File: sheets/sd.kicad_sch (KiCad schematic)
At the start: 1 part

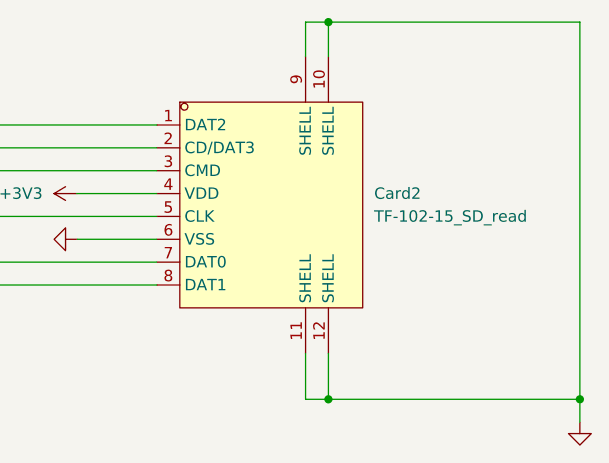
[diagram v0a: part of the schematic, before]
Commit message: added current rush limiting resistors to bmp581
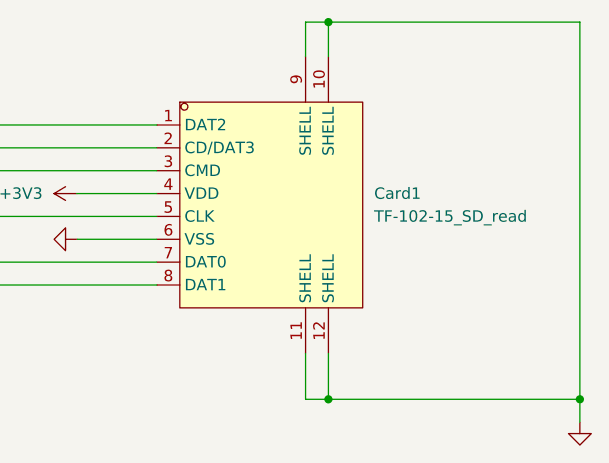
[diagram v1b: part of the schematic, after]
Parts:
- renumbered Card2 to Card1
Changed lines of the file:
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@@
 		)
 		(instances
-			(project ""
+			(project "aerolotl"
 				(path "/3f5bc5ea-feaa-4ed9-b0e0-c918b1fb5754/5163456c-8297-491e-bf51-bada45954a82"
 					(reference "#PWR045")
@@
 		)
 		(instances
-			(project "nc_fc"
+			(project "aerolotl"
 				(path "/3f5bc5ea-feaa-4ed9-b0e0-c918b1fb5754/5163456c-8297-491e-bf51-bada45954a82"
 					(reference "#PWR046")
@@
 		(dnp no)
 		(fields_autoplaced yes)
-		(property "Reference" "Card2"
+		(property "Reference" "Card1"
 			(at 177.8 100.3299 0)
 			(effects
@@
 			(project "aerolotl"
 				(path "/3f5bc5ea-feaa-4ed9-b0e0-c918b1fb5754/5163456c-8297-491e-bf51-bada45954a82"
-					(reference "Card2")
+					(reference "Card1")
 					(unit 1)
 				)
@@
 		)
 		(instances
-			(project ""
+			(project "aerolotl"
 				(path "/3f5bc5ea-feaa-4ed9-b0e0-c918b1fb5754/5163456c-8297-491e-bf51-bada45954a82"
 					(reference "#PWR044")

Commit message: added spi
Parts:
- added R17, R26, R27, R28, R29: 10k, symbol Device:R
- added R30, R31, R32, R33, R34, R35: 10, symbol Device:R
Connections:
- net +3V3: now also R17.1, R26.1, R27.1, R28.1, R29.1
- net SD.CK: now also R33.1; no longer Card1.5 (CLK)
- net SD.CMD: now also R32.1; no longer Card1.3 (CMD)
- net SD.D0: now also R34.1; no longer Card1.7 (DAT0)
- net SD.D1: now also R35.1; no longer Card1.8 (DAT1)
- net SD.D2: now also R30.1; no longer Card1.1 (DAT2)
- net SD.D3: now also R31.1; no longer Card1.2 (CD/DAT3)
- new net: Card1.7 (DAT0), R28.2, R34.2
- new net: Card1.2 (CD/DAT3), R26.2, R31.2
- new net: Card1.8 (DAT1), R29.2, R35.2
- new net: Card1.3 (CMD), R27.2, R32.2
- new net: Card1.1 (DAT2), R17.2, R30.2
- new net: Card1.5 (CLK), R33.2
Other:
- note added: "Note: make trace length short (< 2 inch from MCU to sd card reader)"
- moved on the sheet: Card1

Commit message: Rev1 schematic done
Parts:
- renumbered R35 to R28, R30 to R29, R31 to R30, R32 to R31, R33 to R32, R34 to R33, R29 to R34, R28 to R35, R27 to R36, R26 to R37, R17 to R38
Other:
- moved on the sheet: Card1, R28, R29, R30, R31, R32, R33, R34, R35, R36, R37, R38

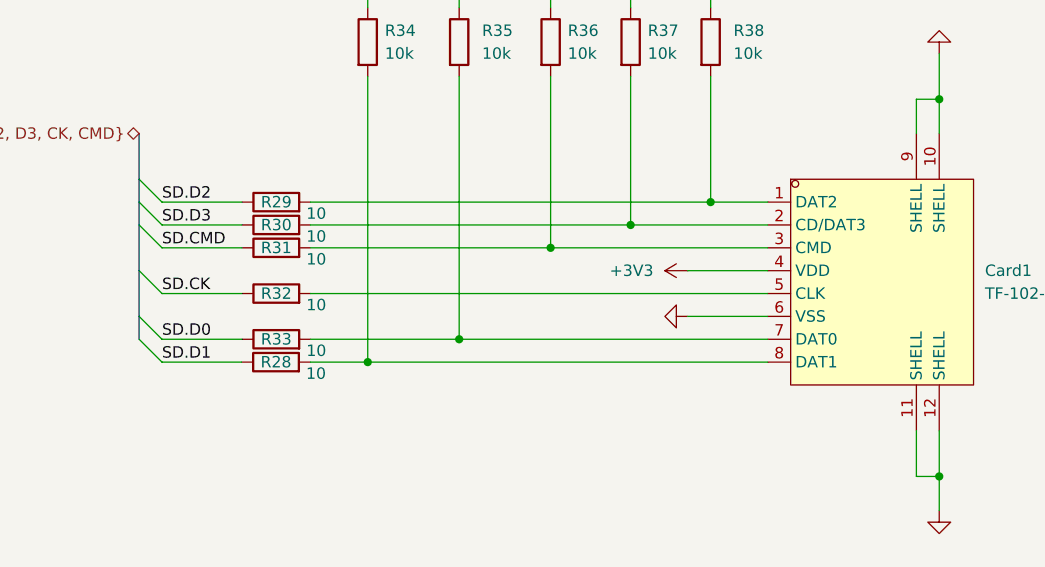
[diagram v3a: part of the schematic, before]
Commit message: Cleared ALL ERC warnings
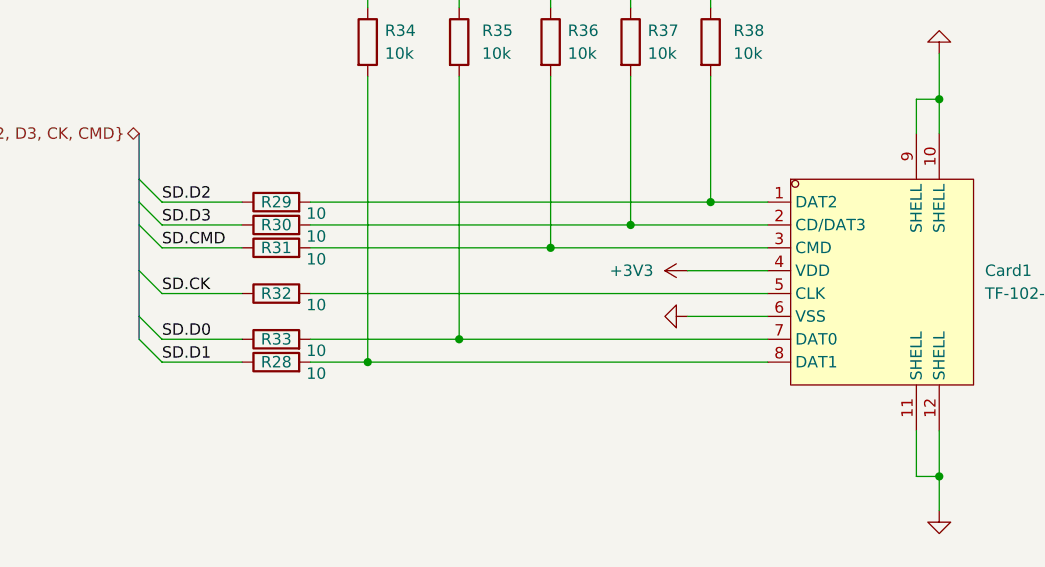
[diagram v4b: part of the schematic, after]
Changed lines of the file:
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@@
 	(wire
 		(pts
-			(xy 114.3 110.49) (xy 123.1579 110.49)
+			(xy 114.3 110.49) (xy 123.19 110.49)
 		)
 		(stroke
@@
 	(wire
 		(pts
-			(xy 130.7779 110.49) (xy 137.16 110.49)
-		)
-		(stroke
-			(width 0)
-			(type default)
-		)
-	)
-	(wire
-		(pts
 			(xy 157.48 71.12) (xy 157.48 64.77)
+		)
+		(stroke
+			(width 0)
+			(type default)
+		)
+	)
+	(wire
+		(pts
+			(xy 130.81 110.49) (xy 137.16 110.49)
 		)
 		(stroke
@@
 	(symbol
 		(lib_id "Device:R")
-		(at 126.9679 110.49 90)
+		(at 127 110.49 90)
 		(unit 1)
 		(exclude_from_sim no)
@@
 		(dnp no)
 		(property "Reference" "R28"
-			(at 126.9679 110.49 90)
+			(at 127 110.49 90)
 			(effects
 				(font
@@
 		)
 		(property "Value" "10"
-			(at 131.4129 111.76 90)
+			(at 131.445 111.76 90)
 			(effects
 				(font
@@
 		)
 		(property "Footprint" ""
-			(at 126.9679 112.268 90)
+			(at 127 112.268 90)
 			(effects
 				(font
@@
 		)
 		(property "Datasheet" "~"
-			(at 126.9679 110.49 0)
+			(at 127 110.49 0)
 			(effects
 				(font
@@
 		)
 		(property "Description" "Resistor"
-			(at 126.9679 110.49 0)
+			(at 127 110.49 0)
 			(effects
 				(font
@@
 	(symbol
 		(lib_id "aerolotl_custom:TF-102-15_SD_read")
-		(at 193.04 101.6 0)
+		(at 194.31 101.6 0)
 		(unit 1)
 		(exclude_from_sim no)
@@
 		)
 		(property "Footprint" "aerolotl_custom:TF-SMD_TF-102-15"
-			(at 193.04 125.73 0)
+			(at 194.31 125.73 0)
 			(effects
 				(font
@@
 		)
 		(property "Datasheet" "https://lcsc.com/product-detail/Connector-Card-Sockets_XUNPU-TF-102-15_C266609.html"
-			(at 193.04 128.27 0)
+			(at 194.31 128.27 0)
 			(effects
 				(font
@@
 		)
 		(property "Description" ""
-			(at 193.04 101.6 0)
+			(at 194.31 101.6 0)
 			(effects
 				(font
@@
 		)
 		(property "LCSC Part" "C266609"
-			(at 193.04 130.81 0)
+			(at 194.31 130.81 0)
 			(effects
 				(font
@@
 		(pin "6"
 		)
+		(pin "5"
+		)
+		(pin "3"
+		)
+		(pin "1"
+		)
+		(pin "2"
+		)
 		(pin "7"
 		)
+		(pin "11"
+		)
+		(pin "12"
+		)
+		(pin "4"
+		)
+		(pin "10"
+		)
 		(pin "8"
 		)
 		(pin "9"
 		)
-		(pin "11"
-		)
-		(pin "5"
-		)
-		(pin "10"
-		)
-		(pin "1"
-		)
-		(pin "12"
-		)
-		(pin "4"
-		)
-		(pin "3"
-		)
-		(pin "2"
-		)
-		(instances
-			(project "aerolotl"
+		(instances
+			(project ""
 				(path "/3f5bc5ea-feaa-4ed9-b0e0-c918b1fb5754/5163456c-8297-491e-bf51-bada45954a82"
 					(reference "Card1")

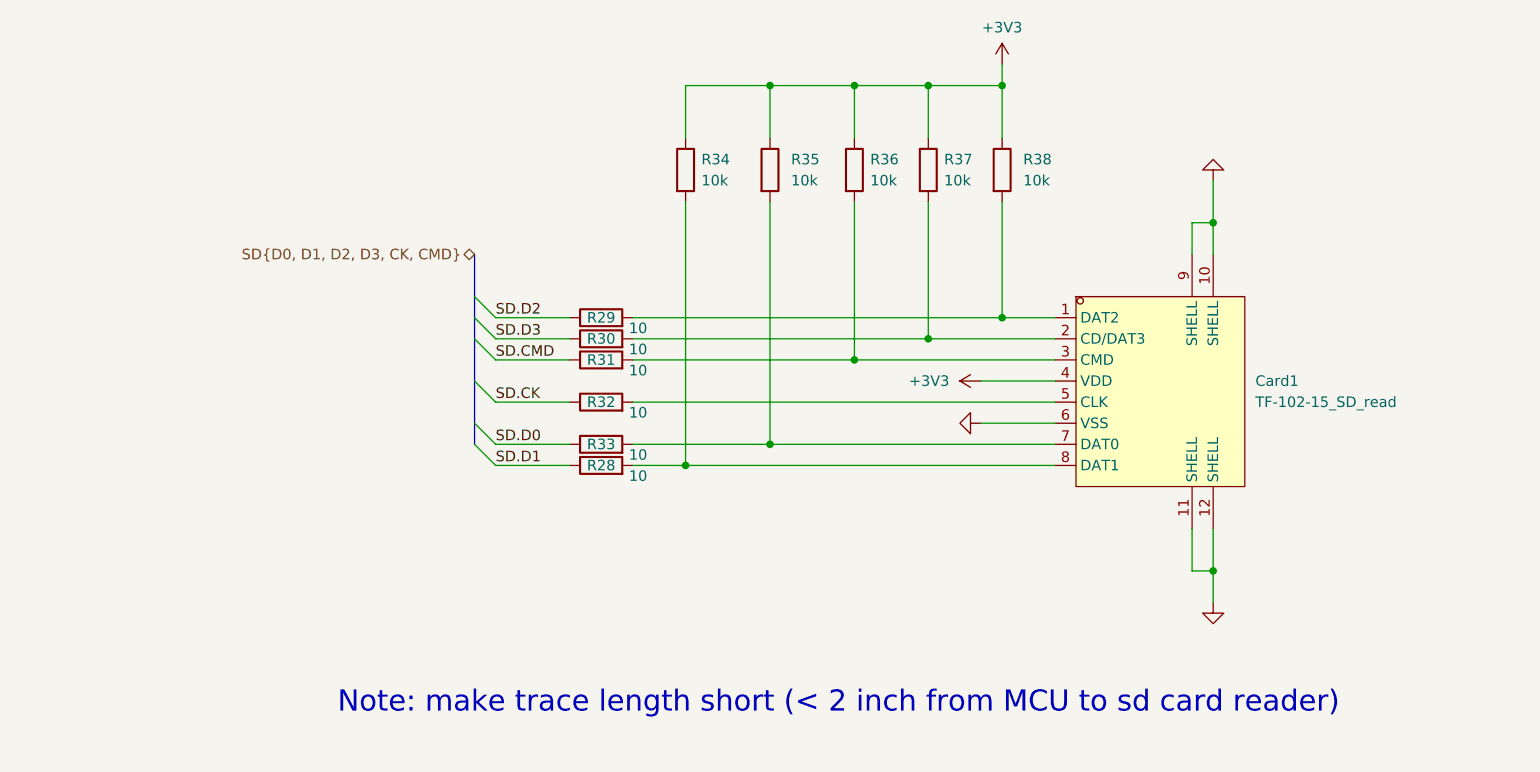
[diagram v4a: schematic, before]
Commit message: letter size schematic pages formatted
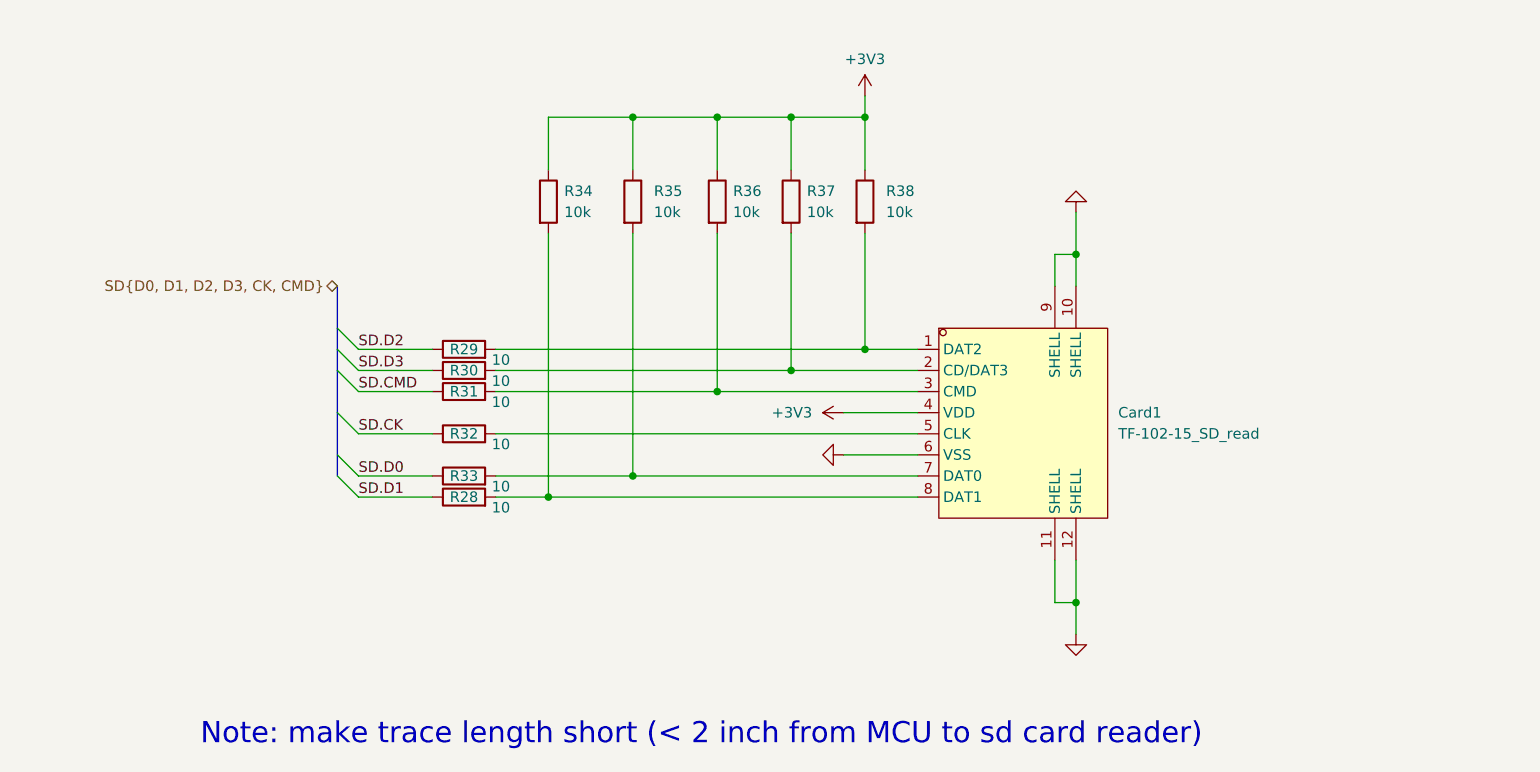
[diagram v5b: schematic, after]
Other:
- moved on the sheet: Card1, R28, R29, R30, R31, R32, R33, R34, R35, R36, R37, R38
